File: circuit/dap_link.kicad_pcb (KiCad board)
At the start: 2 copper layers, 47.1 x 28.5 mm, 32 parts, among them J1 USB_A_CONN, J2 SWD_CONN_5P, J3 UART1_CONN_3P, J5 Conn_02x10_Odd_Even, U1 STM32F103CBTx, U2 AMS1117-3.3, U3 TXS0108EPW, Y1 8MHz

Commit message: 增加圆边
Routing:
- net GND: vias 31 -> 27
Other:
- outline, holes or cut-outs redrawn
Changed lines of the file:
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@@
     )
   )
-  (gr_line (start 138.6 141.8) (end 91.5 141.8)
+  (gr_line (start 138.6 141.8) (end 95.5 141.8)
     (stroke (width 0.05) (type default)) (layer "Edge.Cuts"))
-  (gr_line (start 91.5 113.3) (end 138.6 113.3)
+  (gr_line (start 95.5 113.3) (end 138.6 113.3)
     (stroke (width 0.05) (type default)) (layer "Edge.Cuts"))
-  (gr_line (start 91.5 141.8) (end 91.5 113.3)
+  (gr_line (start 91.5 137.8) (end 91.5 117.3)
     (stroke (width 0.05) (type default)) (layer "Edge.Cuts"))
   (gr_line (start 138.6 113.3) (end 138.6 141.8)
+    (stroke (width 0.05) (type default)) (layer "Edge.Cuts"))
+  (gr_arc (start 91.5 117.3) (mid 92.671573 114.471573) (end 95.5 113.3)
+    (stroke (width 0.05) (type default)) (layer "Edge.Cuts"))
+  (gr_arc (start 95.5 141.8) (mid 92.671573 140.628427) (end 91.5 137.8)
     (stroke (width 0.05) (type default)) (layer "Edge.Cuts"))
   (gr_text "DIO" (at 122.7 134.9) (layer "B.SilkS")
@@
   (via (at 106.602517 130.0045) (size 0.8) (drill 0.4) (layers "F.Cu" "B.Cu") (net 1))
   (via (at 126.275 128.1) (size 0.8) (drill 0.4) (layers "F.Cu" "B.Cu") (net 1))
-  (via (at 94.65 118.5) (size 0.8) (drill 0.4) (layers "F.Cu" "B.Cu") (free) (net 1))
   (via (at 97.925 134.5) (size 0.8) (drill 0.4) (layers "F.Cu" "B.Cu") (net 1))
   (via (at 113.75 116.25) (size 0.8) (drill 0.4) (layers "F.Cu" "B.Cu") (free) (net 1))
@@
   (via (at 130.15 119.5) (size 0.8) (drill 0.4) (layers "F.Cu" "B.Cu") (free) (net 1))
   (via (at 120.925 122.5) (size 0.8) (drill 0.4) (layers "F.Cu" "B.Cu") (net 1))
-  (via (at 96.45 138.95) (size 0.8) (drill 0.4) (layers "F.Cu" "B.Cu") (free) (net 1))
   (via (at 100.45 130.15) (size 0.8) (drill 0.4) (layers "F.Cu" "B.Cu") (free) (net 1))
   (via (at 126.55 133.8) (size 0.8) (drill 0.4) (layers "F.Cu" "B.Cu") (free) (net 1))
@@
   (via (at 110.8 125.8) (size 0.8) (drill 0.4) (layers "F.Cu" "B.Cu") (net 1))
   (via (at 117.9 139.55) (size 0.8) (drill 0.4) (layers "F.Cu" "B.Cu") (free) (net 1))
-  (via (at 99.45 140) (size 0.8) (drill 0.4) (layers "F.Cu" "B.Cu") (free) (net 1))
-  (via (at 96.7 115.85) (size 0.8) (drill 0.4) (layers "F.Cu" "B.Cu") (free) (net 1))
   (via (at 114.7 127.8) (size 0.8) (drill 0.4) (layers "F.Cu" "B.Cu") (net 1))
   (segment (start 98.4625 135.95) (end 98.4625 137.8625) (width 0.5) (layer "B.Cu") (net 1))

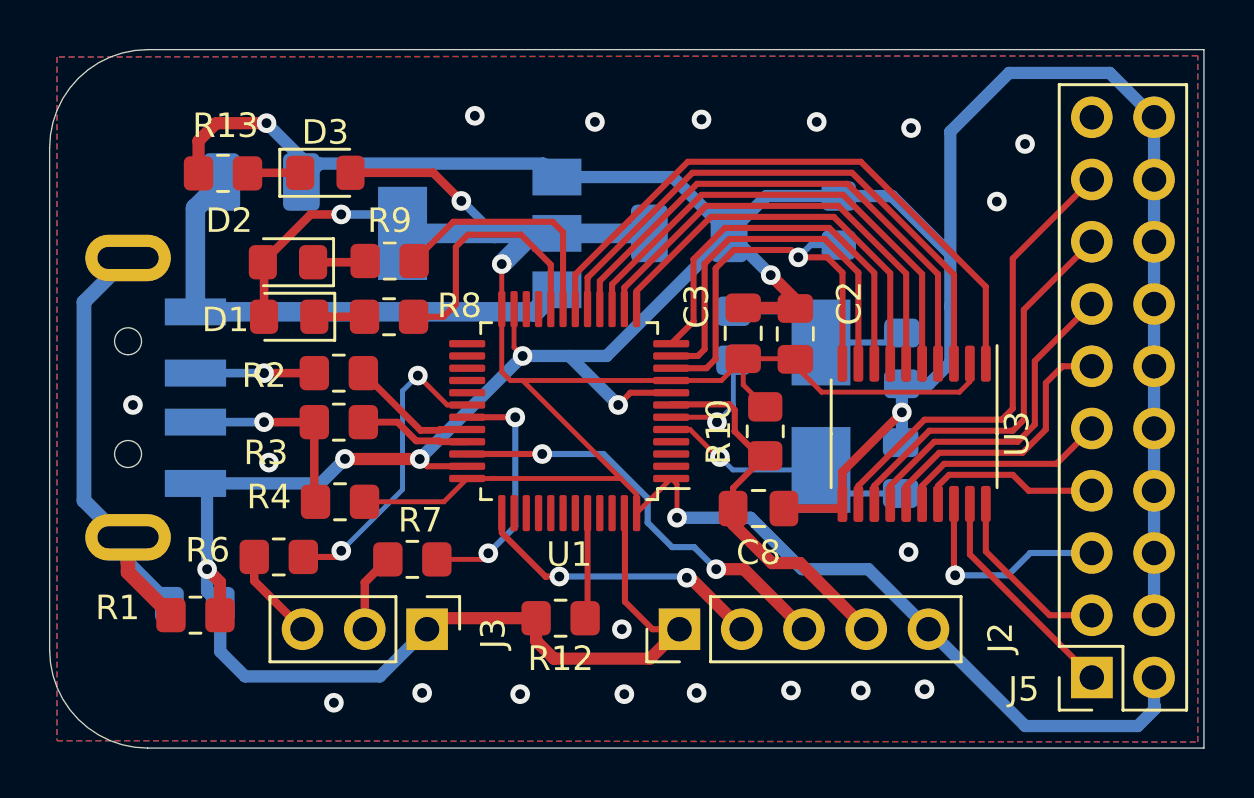
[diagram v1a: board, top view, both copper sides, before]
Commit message: 接口增加一个3.3V
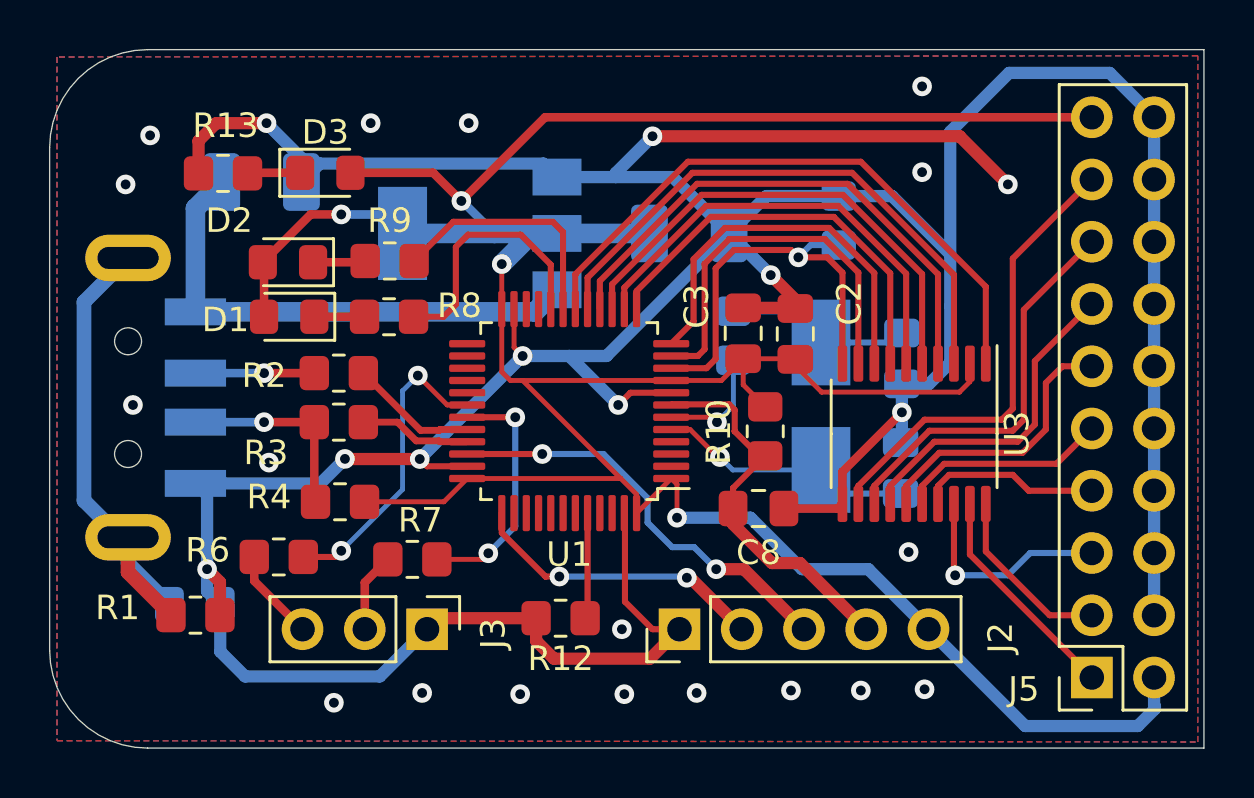
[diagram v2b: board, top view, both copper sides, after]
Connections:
- J5 pad 19: unconnected-(J5-Pin_19-Pad19) -> +3V3
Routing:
- net +3V3: track 103.5 -> 130.6 mm
- net GND: track 167.9 -> 185.5 mm, vias 27 -> 28

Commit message: 增加丝印,缩小USB边距
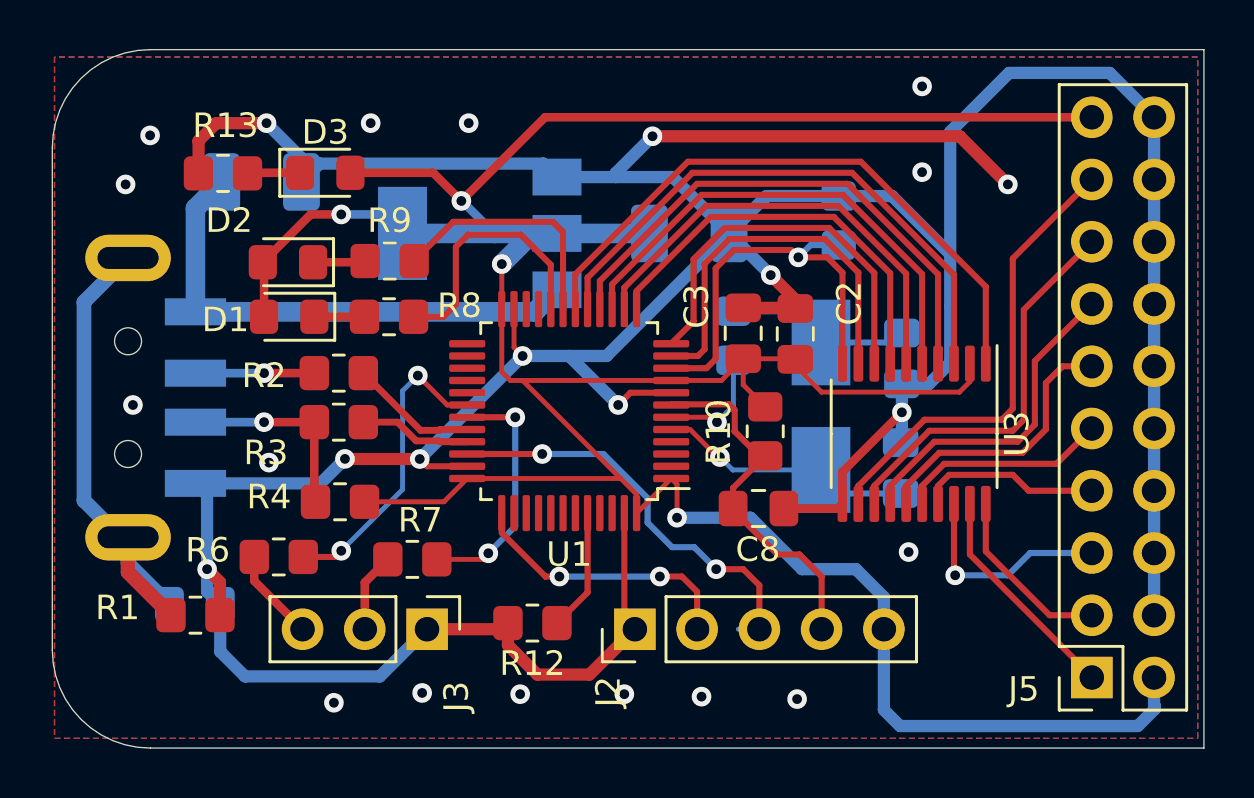
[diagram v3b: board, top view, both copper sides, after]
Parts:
- moved J2 1.82 mm to (115.4, 136.9)
- moved R12 1.17 mm to (111.2, 136.7)
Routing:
- net +3V3: track 130.6 -> 133.3 mm
- net GND: track 185.5 -> 183.3 mm, vias 28 -> 25
- net /SWCLK: track 12.4 -> 11.4 mm
- net /MCU_RST: track 15.8 -> 14.9 mm
- net Net-(U1-BOOT0): track 4.36 -> 5.01 mm
- net /SWDIO: track 17.3 -> 16.7 mm
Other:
- board size 47.1 x 28.5 mm -> 47 x 28.5 mm
- board text added: "3V3"
- board text added: "GND"
- board text added: "NRST"
- board text added: "RCK"
- board text added: "RES"
- board text added: "TCK"
- board text added: "TDI"
- board text added: "TDO"
- board text added: "TMS"
- board text added: "TRST"
- board text added: "VREF"

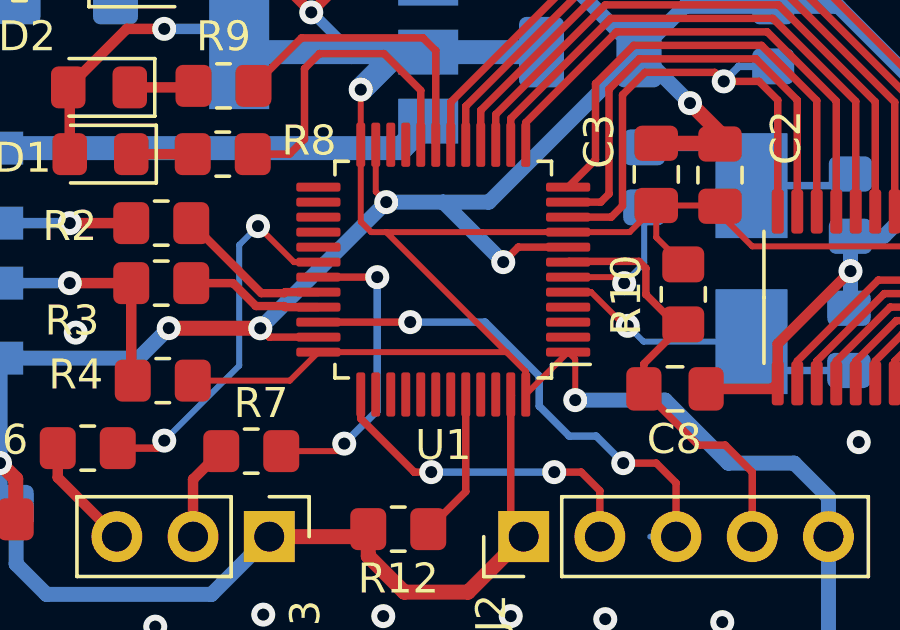
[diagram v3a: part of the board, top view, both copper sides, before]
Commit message: 增加boot按钮
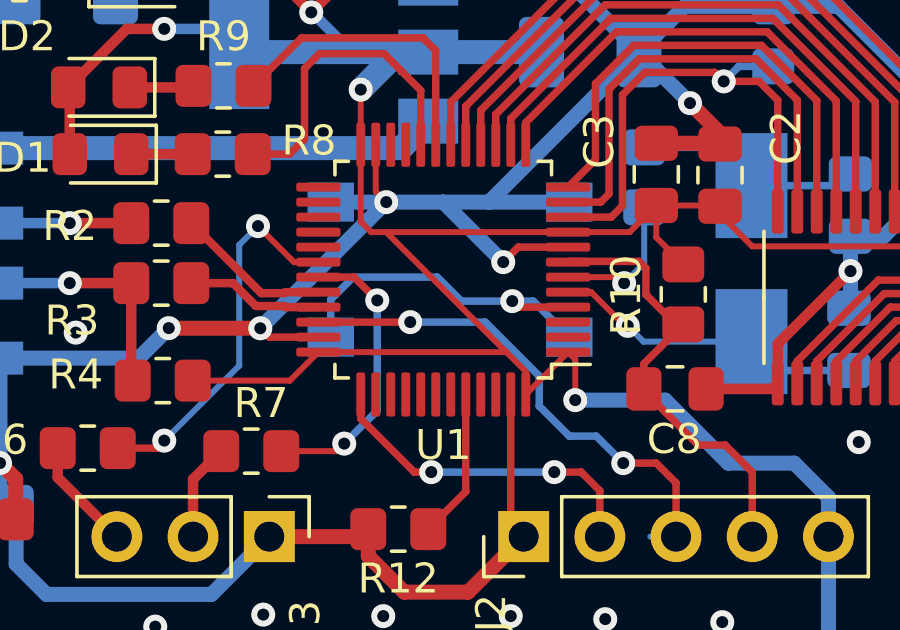
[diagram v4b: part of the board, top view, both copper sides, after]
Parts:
- added SW_Push1: SW_RST, Button_Switch_SMD:SW_Push_1P1T_NO_6x6mm_H9.5mm, B.Cu at (112.9, 128.1)
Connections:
- U1 pad 4: unconnected-(U1-PC15-Pad4) -> /FBOOT
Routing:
- net /FBOOT: track 0.00 -> 12.3 mm, vias 0 -> 1
- net GND: track 183.3 -> 187.9 mm

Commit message: 更新丝印
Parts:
- removed SW_Push1: SW_RST, Button_Switch_SMD:SW_Push_1P1T_NO_6x6mm_H9.5mm
- added SW1: SW_Push, Button_Switch_SMD:SW_Push_1P1T_NO_6x6mm_H9.5mm, B.Cu at (112.9, 128.1)
